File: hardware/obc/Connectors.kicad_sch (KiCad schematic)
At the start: 22 parts, among them J101 Conn_02x20_Odd_Even, J301 USB_C_Receptacle_USB2.0, J302 Conn_High-Rel_4S2P_Vertical, J303 Conn_01x06, J304 Conn_High-Rel_6P

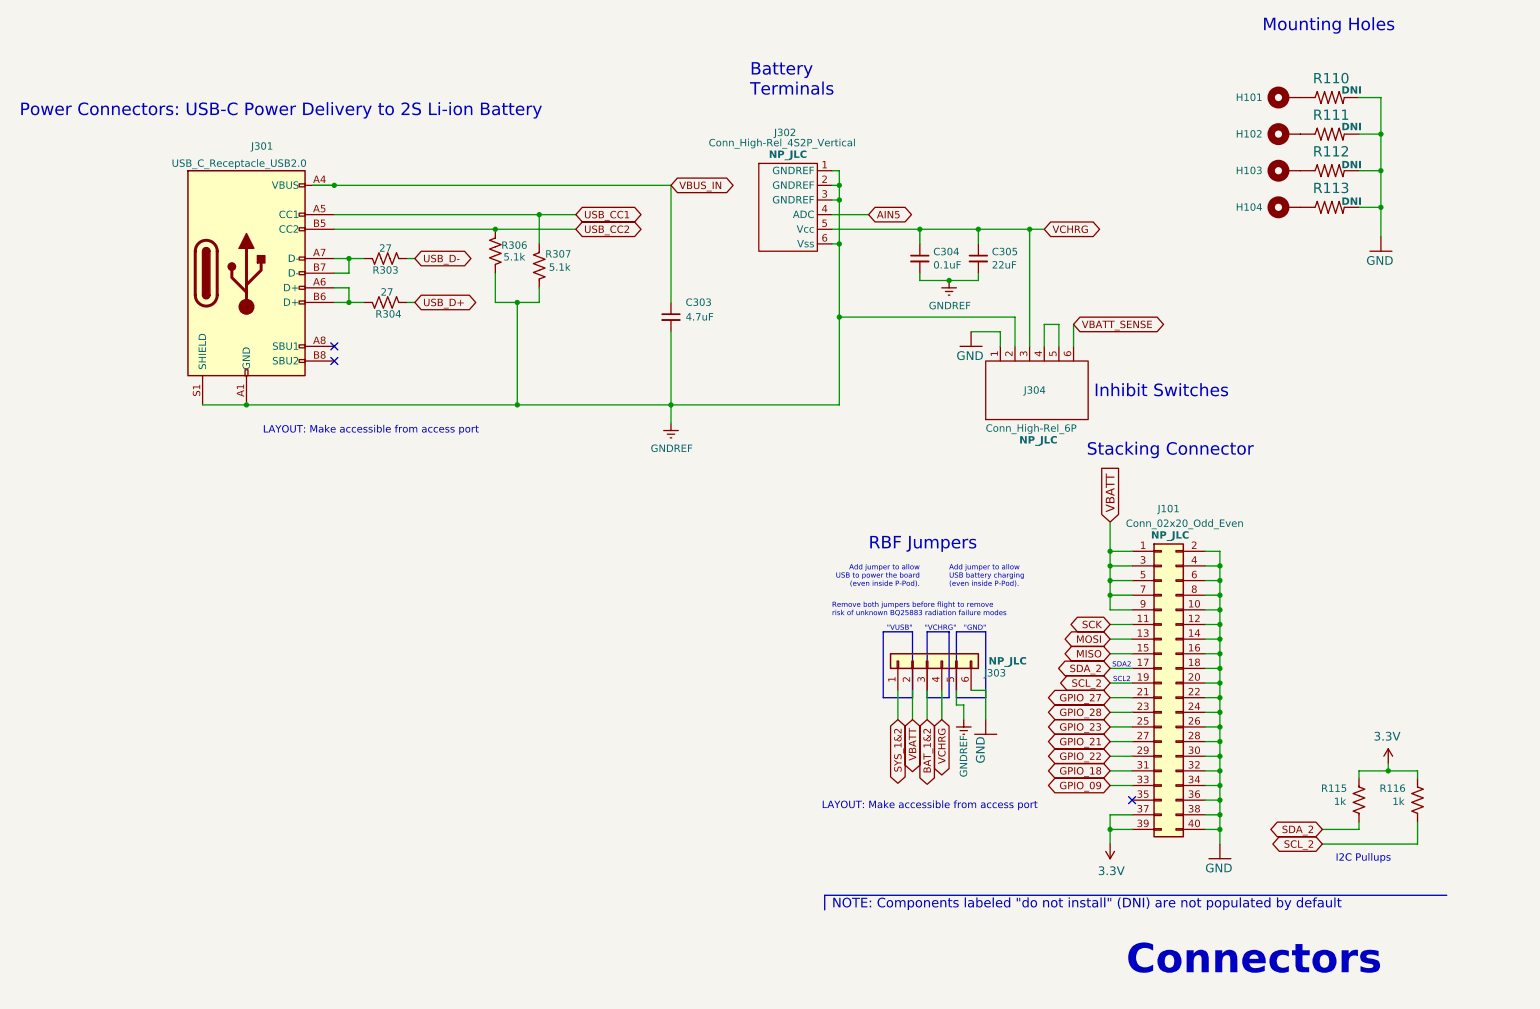
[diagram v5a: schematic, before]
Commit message: obc: final cleanup before review
ex. cleaned wires in PCB, made text nicer on the schematic
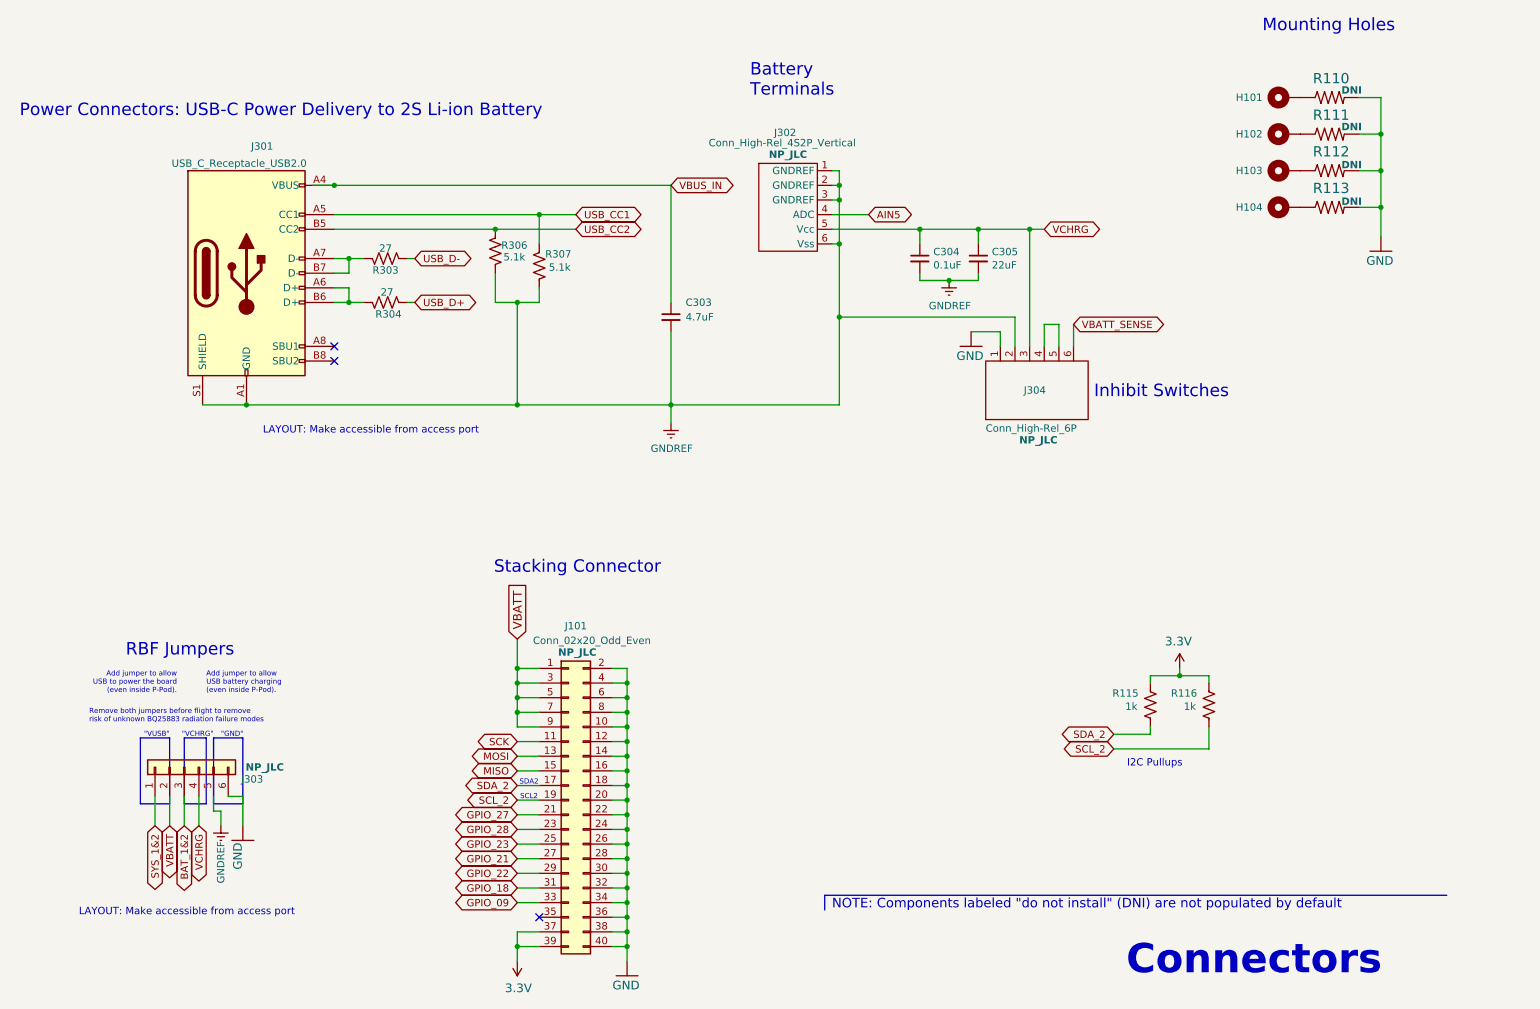
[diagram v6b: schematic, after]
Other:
- moved on the sheet: J101, J303, R115, R116

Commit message: obc: refactors and renumbers
- renumber pages for more logical review order
- renumber reference designators to get smaller numbers
- small changes to layout from early design review
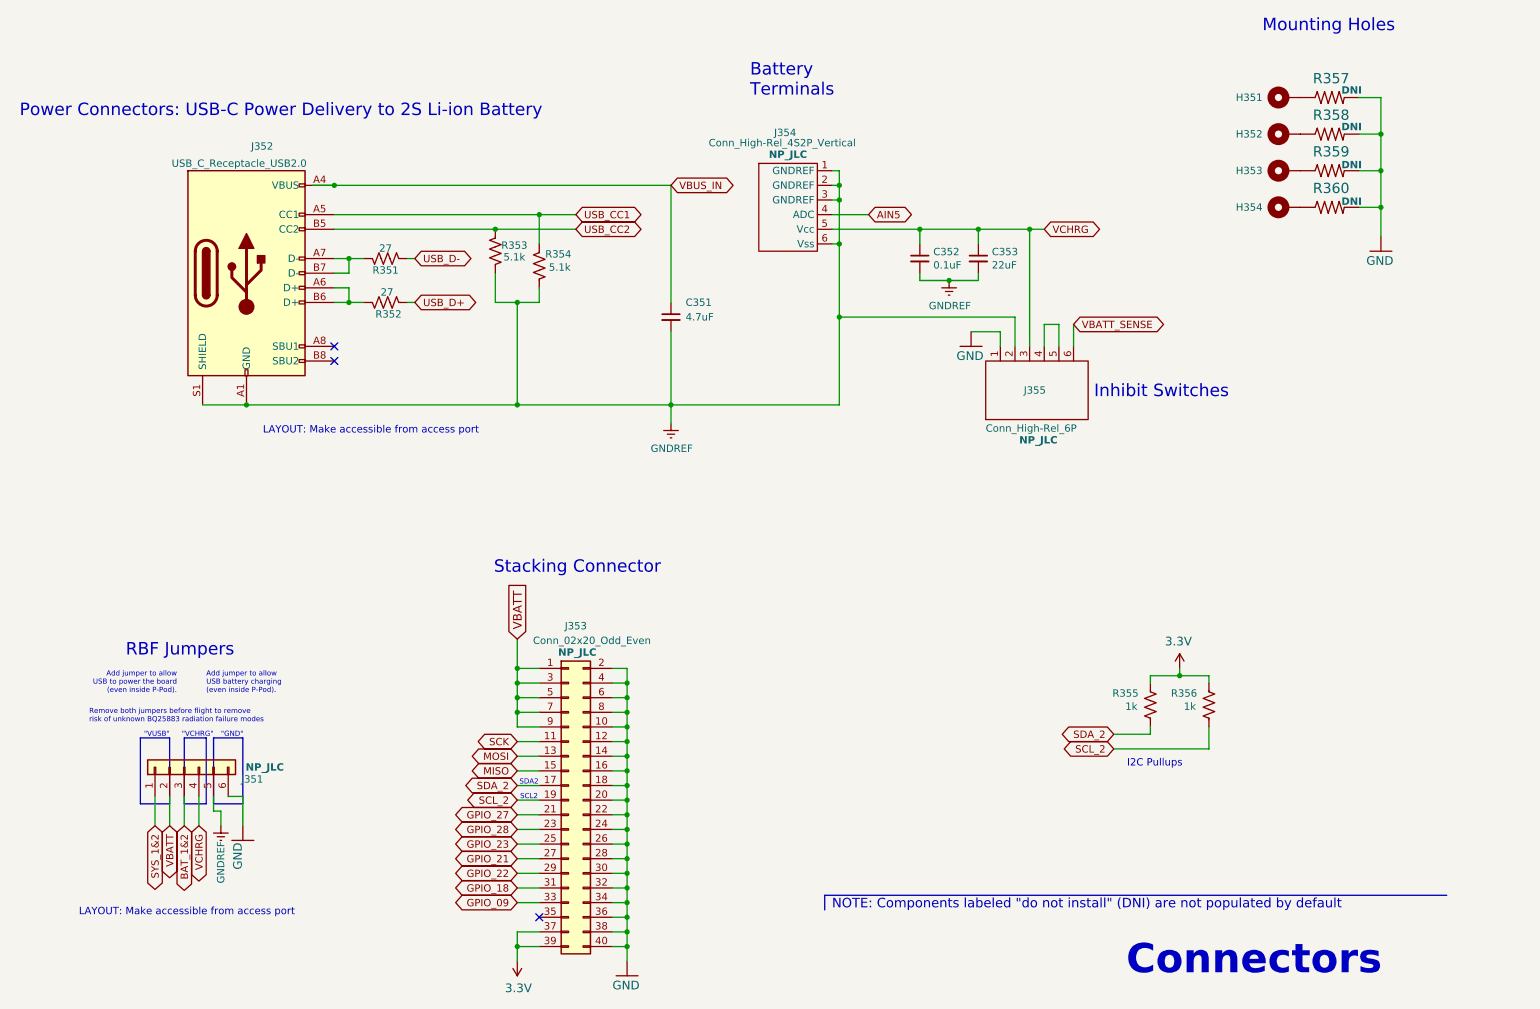
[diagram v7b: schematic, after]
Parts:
- renumbered C303 to C351, C304 to C352, C305 to C353, H101 to H351, H102 to H352, H103 to H353, H104 to H354, J303 to J351, J301 to J352, J101 to J353, J302 to J354, J304 to J355, R303 to R351, R304 to R352, R306 to R353, R307 to R354, R115 to R355, R116 to R356, R110 to R357, R111 to R358, R112 to R359, R113 to R360

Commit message: obc: rename power nets for sanity
We've been confused by this for too long.

GNDREF -> PACKNEG
VCHRG -> PACKPOS
VBATT -> VRAIL
VBATT_SENSE -> INH_POS

Also add an OBC power subsystem diagram.
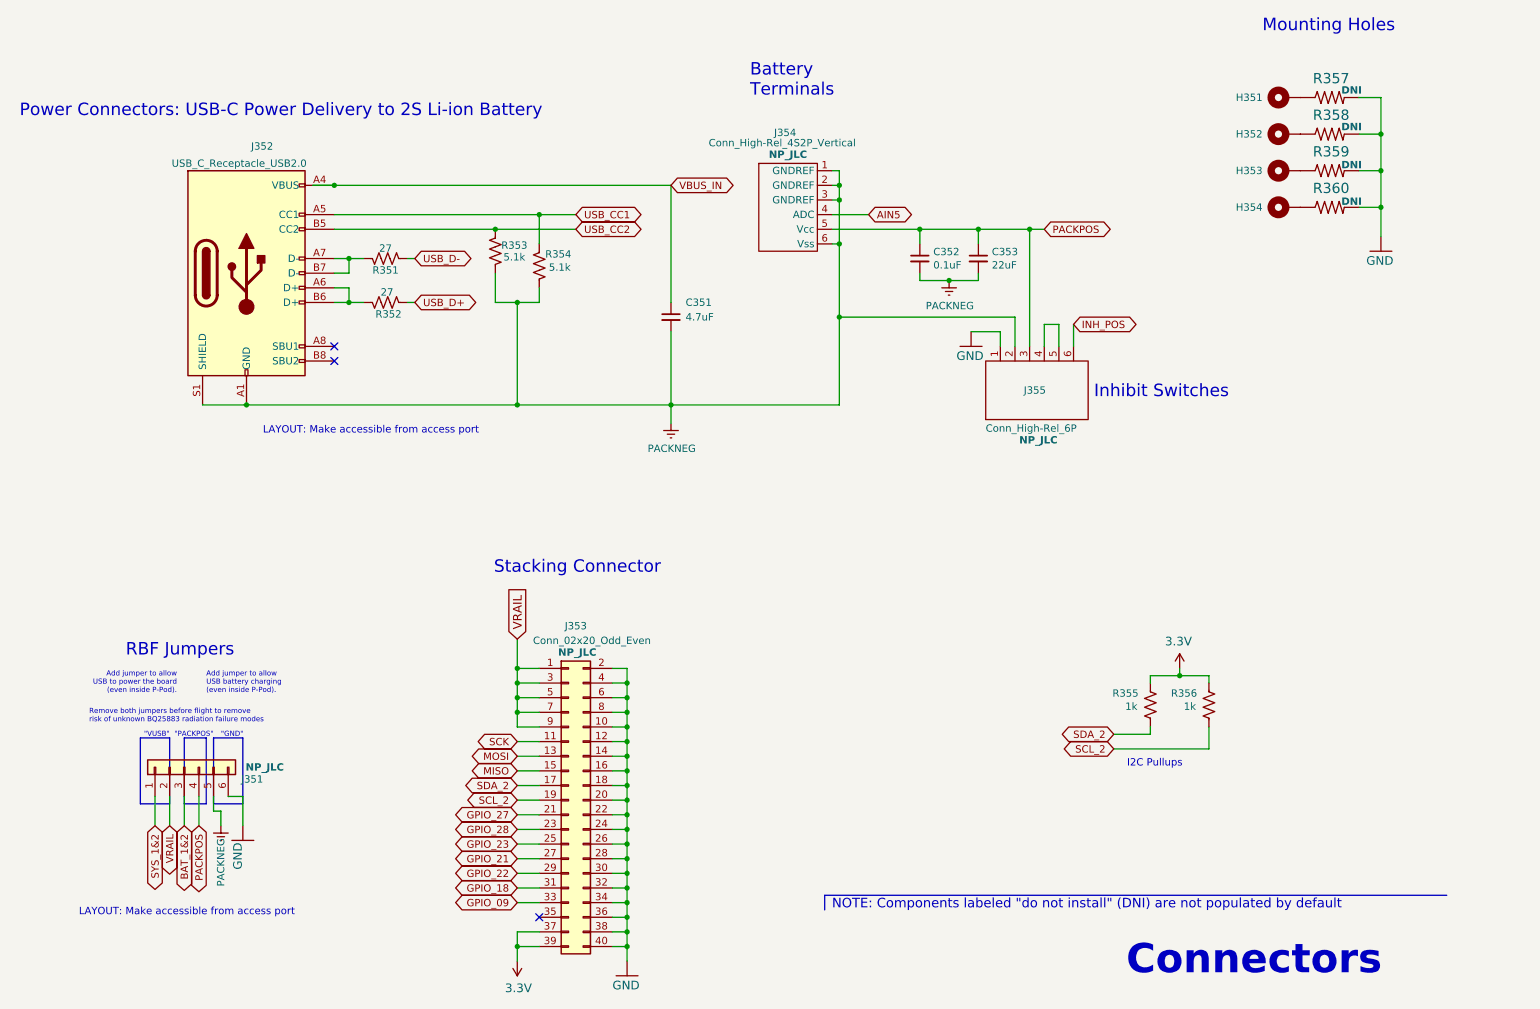
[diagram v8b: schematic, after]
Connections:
- net GNDREF renamed PACKNEG
- net VBATT renamed VRAIL
- net VBATT_SENSE renamed INH_POS
- net VCHRG renamed PACKPOS
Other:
- note added: ""PACKPOS""
- note removed: ""VCHRG""
- note removed: "SCL2"
- note removed: "SDA2"
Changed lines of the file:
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@@
-		)
-	)
-	(text "SCL2"
-		(exclude_from_sim no)
-		(at 107.442 151.892 0)
-		(effects
-			(font
-				(size 0.889 0.889)
-			)
 		)
 	)
@@
 		)
 	)
-	(text "\"VCHRG\""
+	(text "\"PACKPOS\""
 		(exclude_from_sim no)
 		(at 52.705 141.605 0)
@@
 			(font
 				(size 1.27 1.27)
-			)
-		)
-	)
-	(text "SDA2"
-		(exclude_from_sim no)
-		(at 107.442 149.352 0)
-		(effects
-			(font
-				(size 0.889 0.889)
 			)
 		)
@@
 		)
 	)
-	(global_label "VCHRG"
+	(global_label "PACKPOS"
 		(shape bidirectional)
 		(at 50.165 156.845 270)
@@
 		)
 	)
-	(global_label "VBATT_SENSE"
+	(global_label "INH_POS"
 		(shape bidirectional)
 		(at 201.93 69.85 0)
@@
 		)
 	)
-	(global_label "VBATT"
+	(global_label "VRAIL"
 		(shape input)
 		(at 105.41 124.46 90)
@@
 		)
 	)
-	(global_label "VCHRG"
+	(global_label "PACKPOS"
 		(shape bidirectional)
 		(at 196.85 53.34 0)
@@
 		)
 	)
-	(global_label "VBATT"
+	(global_label "VRAIL"
 		(shape bidirectional)
 		(at 45.085 156.845 270)
@@
 			)
 		)
-		(property "Value" "GNDREF"
+		(property "Value" "PACKNEG"
 			(at 132.207 91.3892 0)
 			(effects
@@
 			)
 		)
-		(property "Value" "GNDREF"
+		(property "Value" "PACKNEG"
 			(at 180.467 66.6242 0)
 			(effects
@@
 			)
 		)
-		(property "Value" "GNDREF"
+		(property "Value" "PACKNEG"
 			(at 53.975 163.195 90)
 			(effects
